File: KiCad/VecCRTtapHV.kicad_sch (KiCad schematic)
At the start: 34 parts, among them J1 X, J2 Conn_02x08_Odd_Even, J3 Y, J4 Conn_02x08_Odd_Even, J5 Z, J6 Conn_01x03, J7 Conn_01x03, K1 1UM, Q1 BS250, Q2 BS170, Y1 3mm, Y2 3mm, Y3 3mm, Y4 3mm

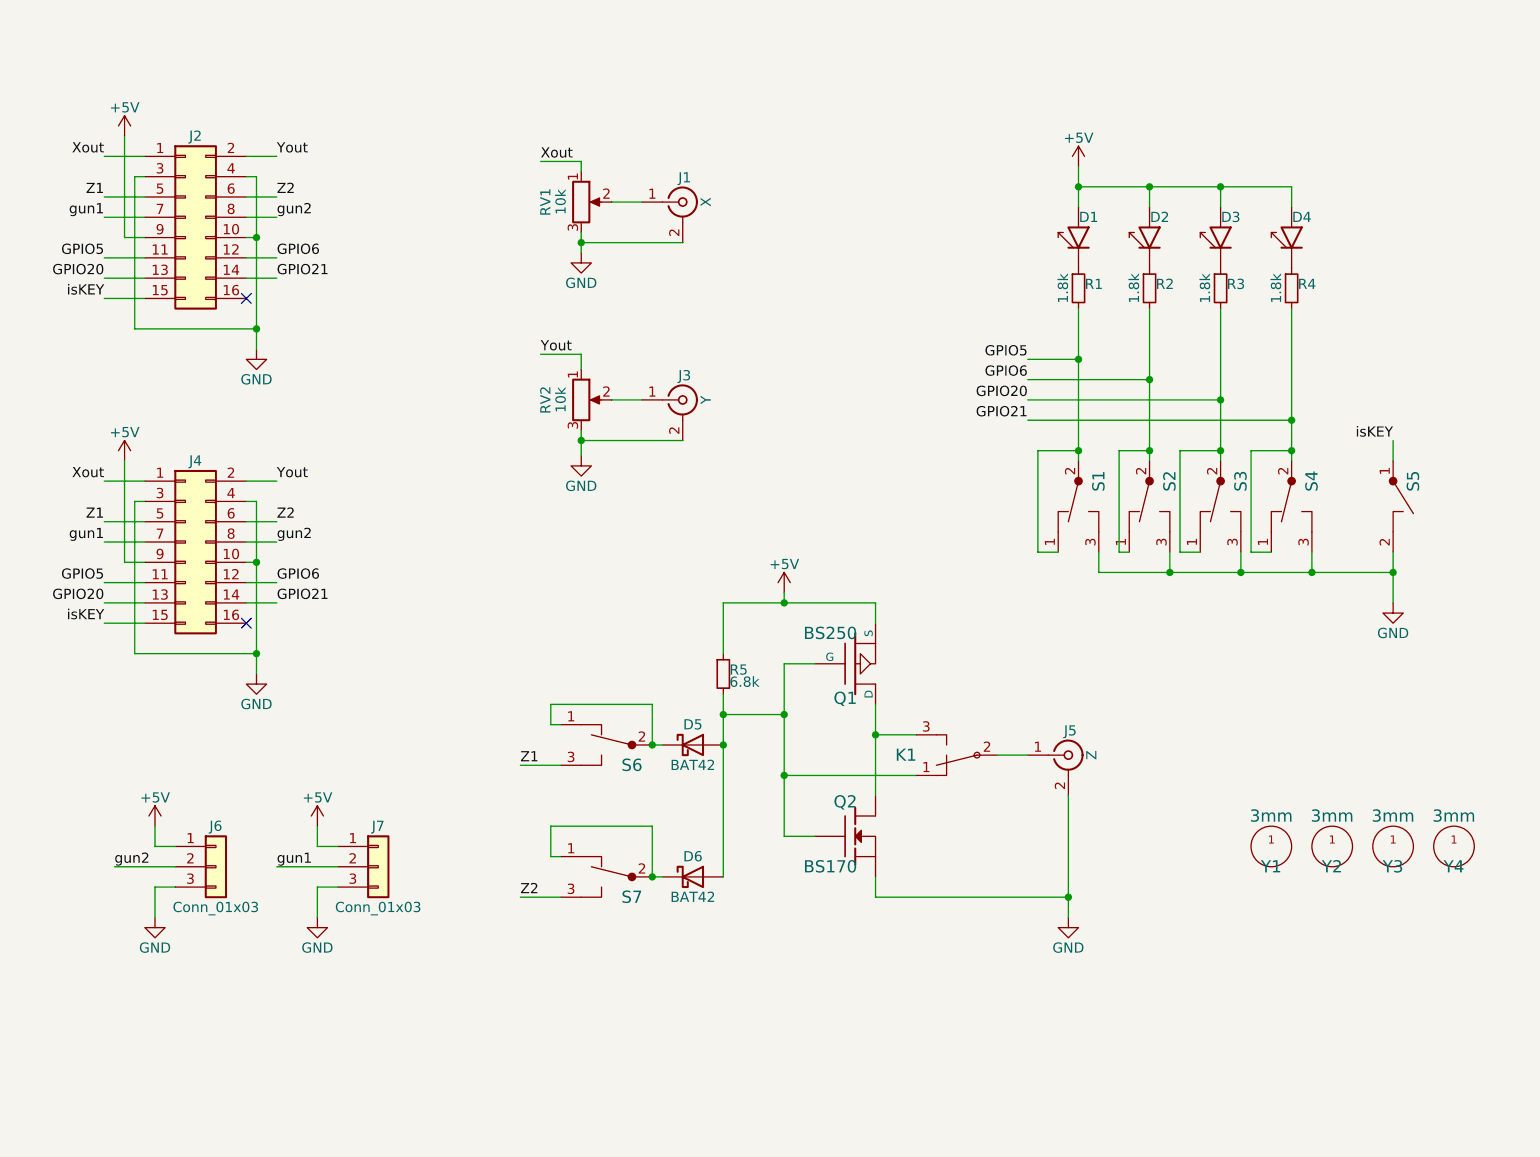
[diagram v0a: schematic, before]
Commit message: Update lightgun LED, add HV, fixes
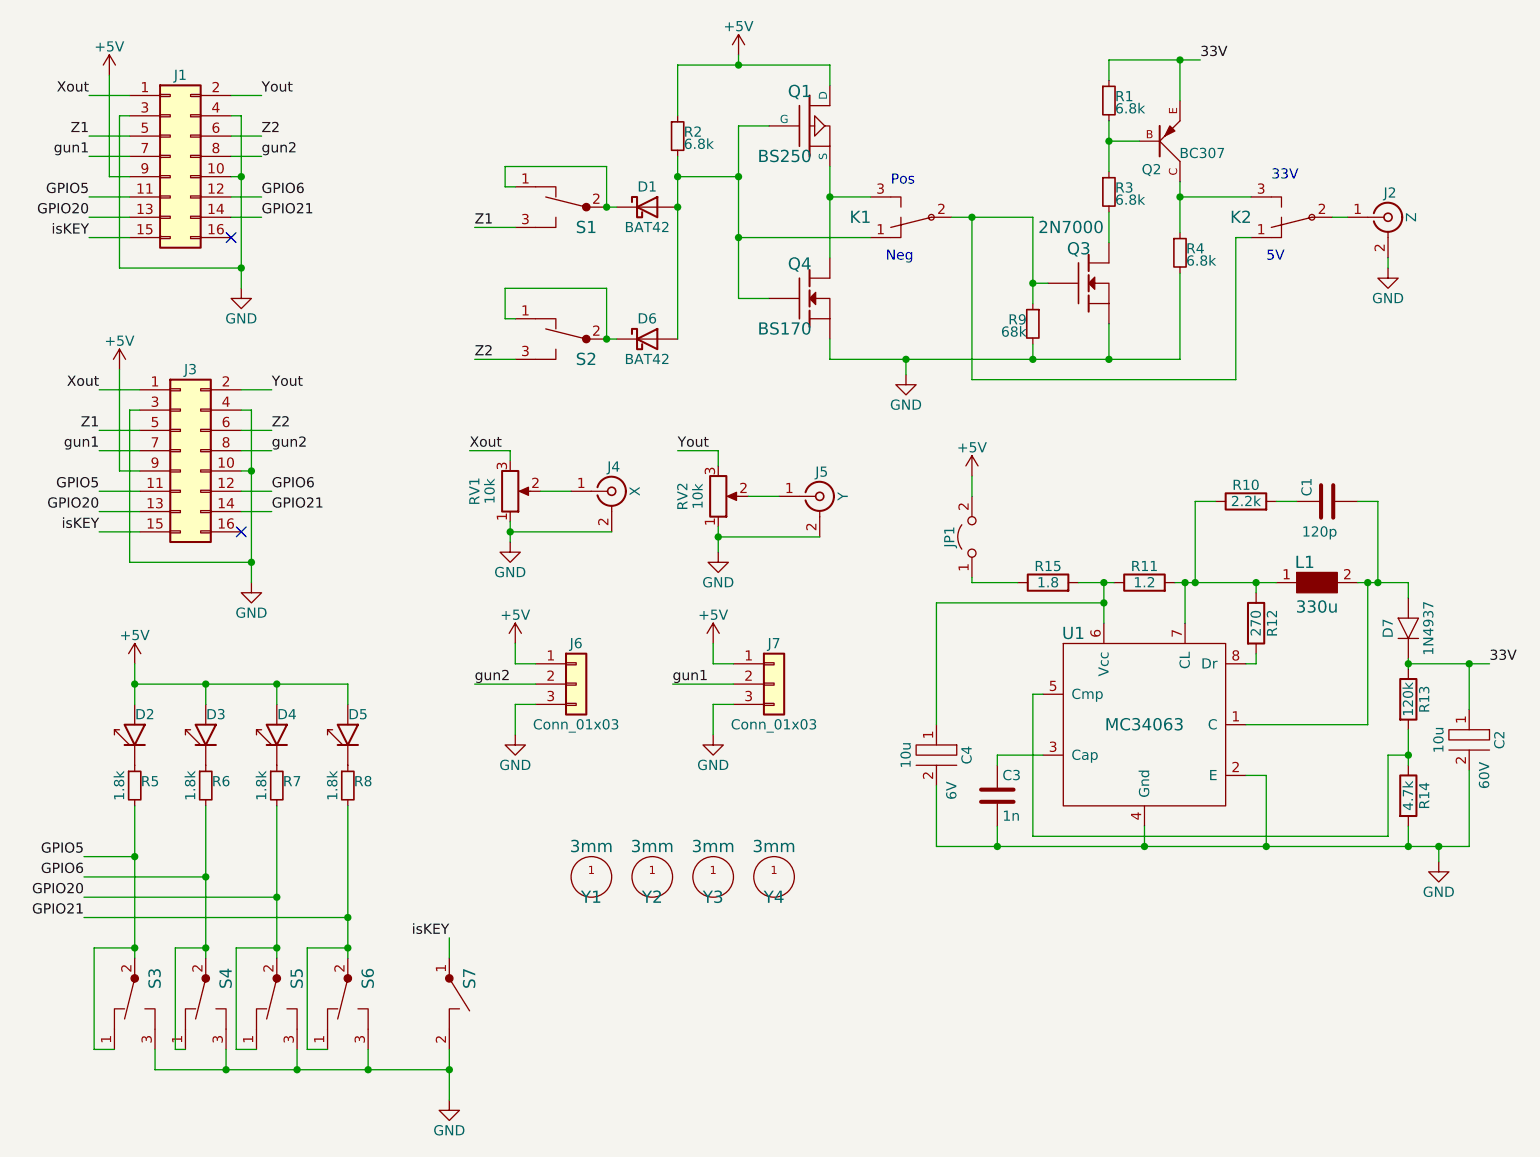
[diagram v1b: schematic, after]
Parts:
- added C1: 120p, RG:C2-2, symbol Device:C
- added C2, C4: 10u, RG:C2-7, symbol rg:ELKO
- added C3: 1n, RG:C2-2, symbol Device:C
- added D7: 1N4937, Diode_THT:D_DO-35_SOD27_P7.62mm_Horizontal, symbol rg:1N4448
- added JP1: Jumper_2_Open, RG:Pins_2, symbol Jumper:Jumper_2_Open
- added K2: 1UM, RG:Pins_3, symbol rg:1UM
- added L1: 330u, RG:C2-7, symbol rg:INDUCTOR
- added Q2: BC307, RG:TO-92_RG_EBC, symbol rg:BC307
- added Q3: 2N7000, RG:FETsgd_inline, symbol rg:BS170
- added R1, R3, R4: 6.8k, RG:R4-2, symbol Device:R_Small
- added R10: 2.2k, RG:R4-2, symbol Device:R
- added R11: 1.2, RG:R4-2, symbol Device:R
- added R12: 270, RG:R4-2, symbol Device:R
- added R13: 120k, RG:R4-2, symbol Device:R
- added R14: 4.7k, RG:R4-2, symbol Device:R
- added R15: 1.8, RG:R4-2, symbol Device:R
- added R9: 68k, RG:R4-2, symbol Device:R_Small
- added U1: MC34063, RG:DIP-8_300, symbol rg:MC34063
- Q1: footprint RG:FETdgs_inline -> RG:FETsgd_inline
- Q4: renamed from Q2; footprint RG:FETdgs_inline -> RG:FETsgd_inline
- renumbered D5 to D1, D1 to D2, D2 to D3, D3 to D4, D4 to D5, J2 to J1, J5 to J2, J4 to J3, J1 to J4, J3 to J5, R5 to R2, R1 to R5, R2 to R6, R3 to R7, R4 to R8, S6 to S1, S7 to S2, S1 to S3, S2 to S4, S3 to S5, S4 to S6, S5 to S7
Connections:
- net +5V: now also Q1.D, JP1.2 (B); no longer Q1.S
- net GND: now also RV1.1, RV2.1, C2.2, C3.2, C4.2, Q3.S, R14.2, R4.2, R9.2, U1.2 (E), U1.4 (Gnd); no longer RV1.3, RV2.3
- net Xout: now also RV1.3; no longer RV1.1
- net Yout: now also RV2.3; no longer RV2.1
- net at K1.3, Q4.D: now also Q1.S; no longer Q1.D
- net at K1.2: now also K2.1, Q3.G, R9.1; no longer J2.1 (In)
- new net: JP1.1 (A), R15.1
- new net: C4.1, R11.1, R15.2, U1.6 (Vcc)
- new net: Q2.B, R1.2, R3.1
- new net: Q3.D, R3.2
- new net: J2.1 (In), K2.2
- new net: K2.3, Q2.C, R4.1
- new net: L1.1, R10.1, R11.2, R12.1, U1.7 (CL)
- new net: C1.2, D7.2 (A), L1.2, U1.1 (C)
- new net: C1.1, R10.2
- new net: C3.1, U1.3 (Cap)
- new net: R13.2, R14.1, U1.5 (Cmp)
- new net: R12.2, U1.8 (Dr)
- new net 33V: C2.1, D7.1 (K), Q2.E, R1.1, R13.1
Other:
- note added: "33V"
- note added: "5V"
- note added: "Neg"
- note added: "Pos"
- title: WWI Vectors: Display Tap -> WWI Vectors: Display Tap with Higher-Voltage Z
- moved on the sheet: D1, D2, D3, D4, D5, D6, J1, J2, J3, J4, J5, J6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

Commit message: small fixes
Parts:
- C4: value 10u -> 470u
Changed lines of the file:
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@@
     (in_bom yes) (on_board yes)
     (property "Reference" "C4" (id 0) (at 128.27 95.25 0))
-    (property "Value" "10u" (id 1) (at 120.65 95.25 0))
+    (property "Value" "470u" (id 1) (at 120.65 95.25 0))
     (property "Footprint" "RG:C2-7" (id 2) (at 124.46 96.52 0)
       (effects (font (size 1.524 1.524)) hide)
@@
     )
     (path "/e81faa2b-80b4-4e8b-af0d-4a14b22fc084"
-      (reference "C4") (unit 1) (value "10u") (footprint "RG:C2-7")
+      (reference "C4") (unit 1) (value "470u") (footprint "RG:C2-7")
     )
     (path "/e359ff2d-c7b7-40be-9b2f-63774d5791ca"
